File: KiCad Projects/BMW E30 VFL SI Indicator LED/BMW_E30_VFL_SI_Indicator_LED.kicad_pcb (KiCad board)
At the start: 2 copper layers, 58 x 32.4 mm, 15 parts, among them J1 Conn_01x13_Socket

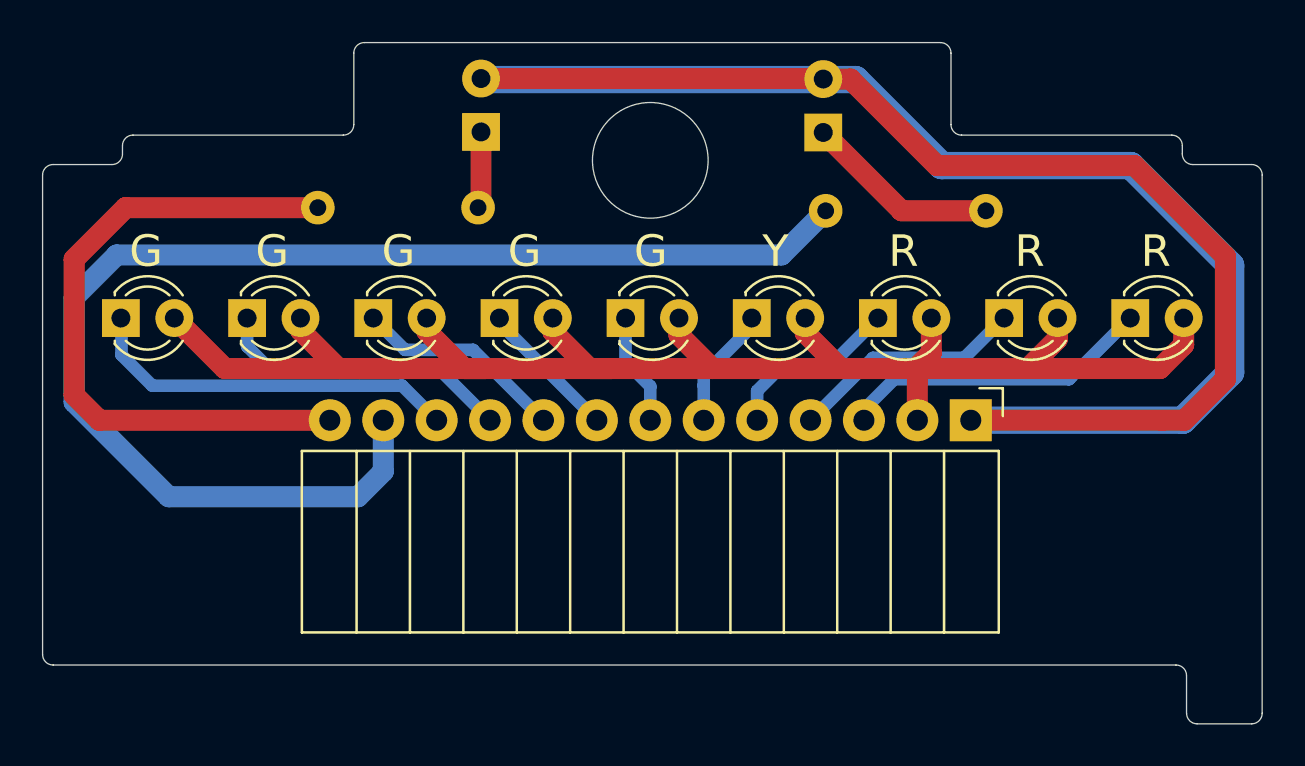
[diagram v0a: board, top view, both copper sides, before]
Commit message: Increase mounting hole diameter to 6.5mm
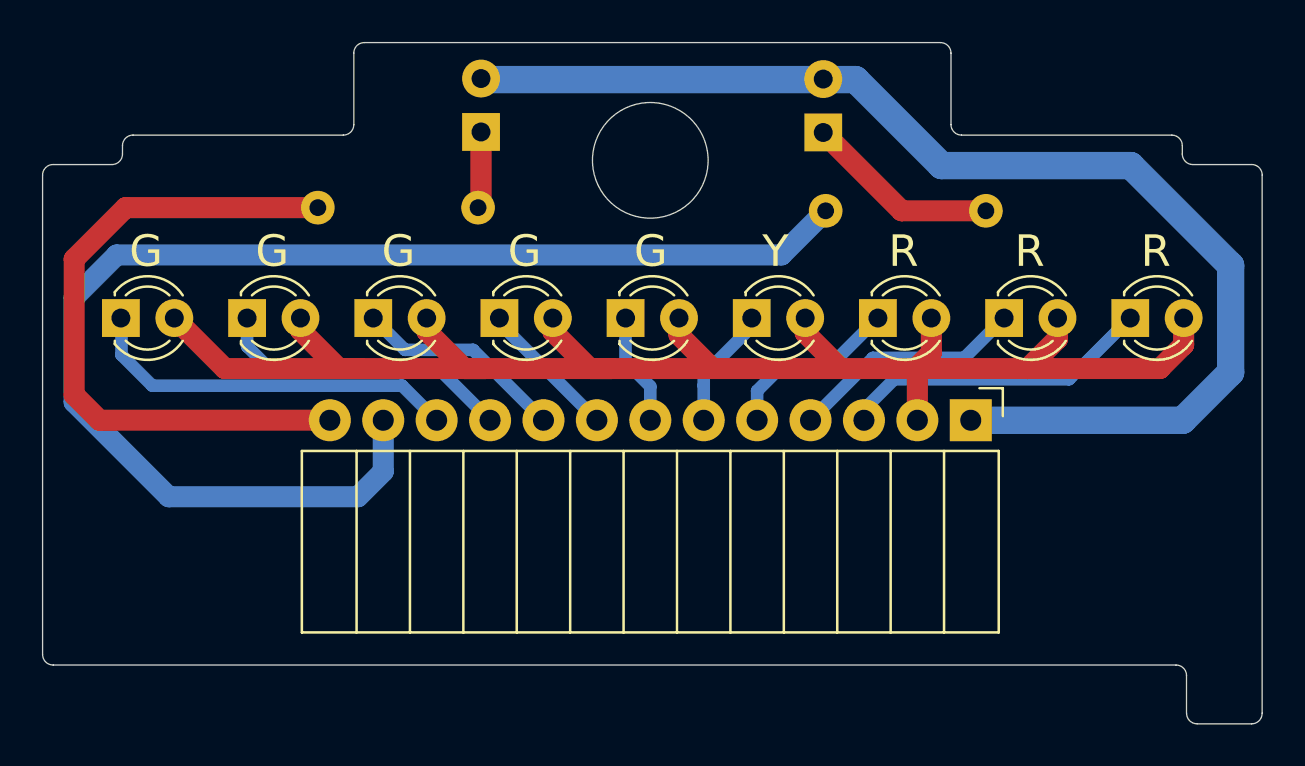
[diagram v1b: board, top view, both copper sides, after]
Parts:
- R1, R2: value 160R -> 510R
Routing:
- net Net-(D10-A): track 115.4 -> 57.7 mm
